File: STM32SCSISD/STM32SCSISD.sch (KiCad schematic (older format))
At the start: 19 parts, among them J1 SERIAL_DEBUG, J2 SWD, J3 USB, J4 SCSI, J5 ACTIVITYLED, J6 AMP FLOPPY PWR, J7 Micro_SD_Card_Det_Hirose_DM3AT, U1 STM32F103C8Tx, U2 MIC5504-3.3YM5, Y1 8MHz

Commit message: Pre-review of schematic.
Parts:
- added C10, C6, C7, C8, C9: 0.1u, symbol Device:C_Small
- added C3, C4, C5: 1u, symbol Device:C_Small
- added R1, R2: 22, symbol Device:R_Small
- added R10, R11, R6, R9: 10k, symbol Device:R_Small
- added R3: 4.7k, symbol Device:R_Small
- added R5: 470, symbol Device:R_Small
- added R7, R8: 47k, symbol Device:R_Small
- gave numbers to parts that had none: 3
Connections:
- net labels added: +5V, RESET, SD_CLK, SD_CS, SD_MISO, SD_MOSI, SERIAL_RX, SERIAL_TX, SWDCLK, SWDIO, UNIT_SEL2, USB+, USB-
- wire segments 114 -> 254
- no-connect marks 0 -> 7
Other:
- moved on the sheet: J6, JP1, JP2, JP3, JP5, JP6

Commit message: Hope this board looks nice!
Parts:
- removed R10, R11, R9: 10k, symbol Device:R_Small
- added C11: 47u, Capacitor_THT:CP_Radial_D5.0mm_P2.50mm, symbol Device:CP_Small
- added JP7: UNITSEL0, Connector_PinHeader_2.54mm:PinHeader_1x02_P2.54mm_Vertical, symbol Device:Jumper
- added JP8: UNITSEL1, Connector_PinHeader_2.54mm:PinHeader_1x02_P2.54mm_Vertical, symbol Device:Jumper
- C1, C10, C2, C3, C4, C5, C6, C7, C8, C9: footprint (none) -> Capacitor_SMD:C_0805_2012Metric
- J1: footprint (none) -> Connector_PinHeader_2.54mm:PinHeader_1x03_P2.54mm_Vertical
- J2, J3: footprint (none) -> Connector_PinHeader_2.54mm:PinHeader_1x04_P2.54mm_Vertical
- J4: footprint (none) -> Connector_IDC:IDC-Header_2x25_P2.54mm_Vertical
- J5, JP3, JP4, JP5, JP6: footprint (none) -> Connector_PinHeader_2.54mm:PinHeader_1x02_P2.54mm_Vertical
- J6: footprint (none) -> General:TE_MATE-N-LOK_350211-1_1x04_P5.08mm_Vertical
- J7: footprint (none) -> Connector_Card:microSD_HC_Hirose_DM3AT-SF-PEJM5
- JP1: value UNITSEL0 -> IMAGE_SEL0; footprint (none) -> Connector_PinHeader_2.54mm:PinHeader_1x02_P2.54mm_Vertical
- JP2: value UNITSEL1 -> IMAGE_SEL1; footprint (none) -> Connector_PinHeader_2.54mm:PinHeader_1x02_P2.54mm_Vertical
- R1, R2, R3, R4, R5, R6, R7, R8: footprint (none) -> Resistor_SMD:R_0805_2012Metric_Pad1.15x1.40mm_HandSolder
- Y1: footprint (none) -> Crystal:Crystal_HC49-U_Vertical
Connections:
- net labels added: IMAGE_SEL0, IMAGE_SEL1
- wire segments 254 -> 244
- no-connect marks 7 -> 10
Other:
- moved on the sheet: JP1, JP2

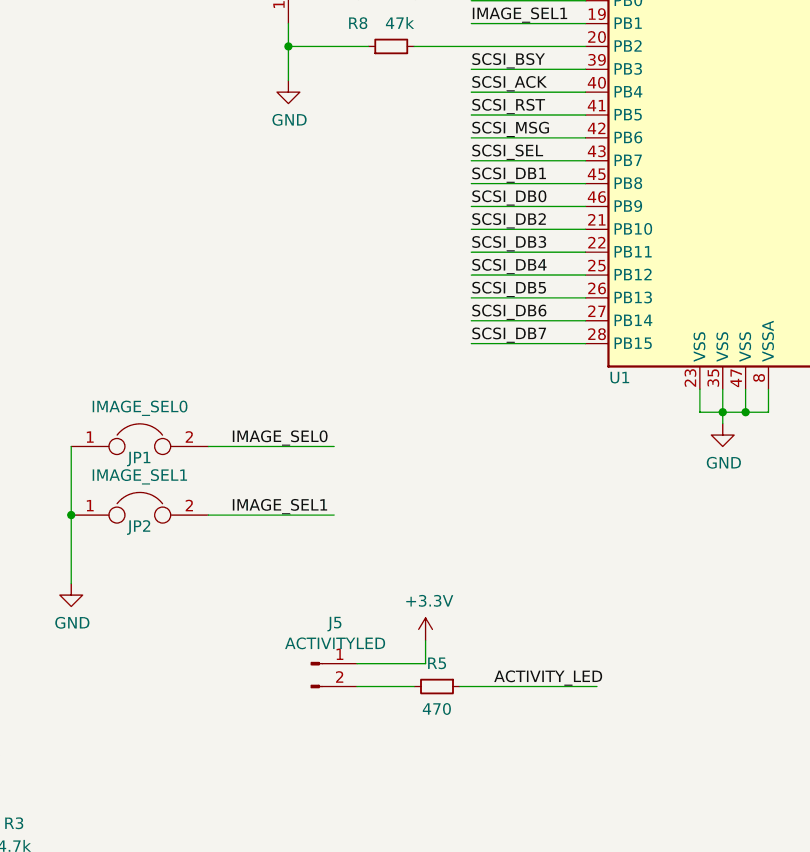
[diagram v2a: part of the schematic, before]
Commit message: Fixed the two SCSI databus bit that was mixed up. Added a 5mm LED instead of connector.
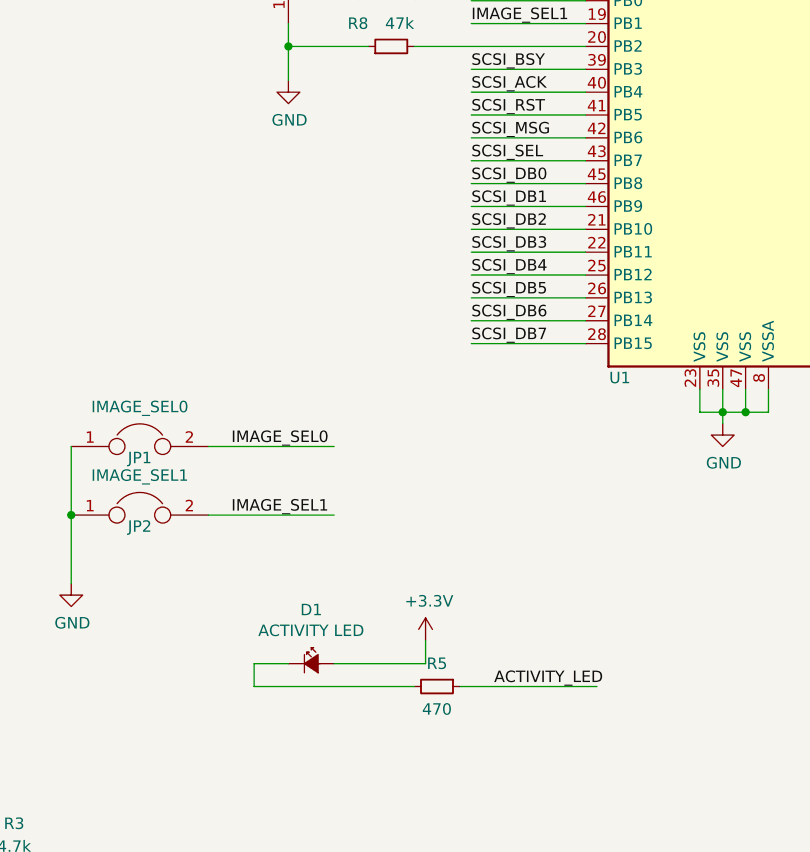
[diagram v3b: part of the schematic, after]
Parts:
- removed J5: ACTIVITYLED, Connector_PinHeader_2.54mm:PinHeader_1x02_P2.54mm_Vertical, symbol Connector:Conn_01x02_Male
- added D1: ACTIVITY LED, symbol Device:LED_Small_ALT
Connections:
- wire segments 244 -> 246
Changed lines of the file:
@@
-$EndComp
-$Comp
-L Connector:Conn_01x04_Male J3
-U 1 1 5FC2CB36
-P 1500 6850
-F 0 "J3" H 1606 7128 50  0000 C CNN
-F 1 "USB" H 1606 7037 50  0000 C CNN
-F 2 "Connector_PinHeader_2.54mm:PinHeader_1x04_P2.54mm_Vertical" H 1500 6850 50  0001 C CNN
-F 3 "~" H 1500 6850 50  0001 C CNN
-	1    1500 6850
-	1    0    0    -1
 $EndComp
 $Comp
@@
 F 3 "~" H 6450 6050 50  0001 C CNN
 	1    6450 6050
-	1    0    0    -1
-$EndComp
-$Comp
-L Connector:Conn_01x02_Male J5
-U 1 1 5FC2D24F
-P 3850 5800
-F 0 "J5" H 3956 5978 50  0000 C CNN
-F 1 "ACTIVITYLED" H 3956 5887 50  0000 C CNN
-F 2 "Connector_PinHeader_2.54mm:PinHeader_1x02_P2.54mm_Vertical" H 3850 5800 50  0001 C CNN
-F 3 "~" H 3850 5800 50  0001 C CNN
-	1    3850 5800
 	1    0    0    -1
 $EndComp
@@
 $EndComp
 Wire Wire Line
-	1700 6750 1950 6750
-Wire Wire Line
-	1700 7050 1800 7050
-Wire Wire Line
-	1800 7050 1800 7150
-Wire Wire Line
 	1650 6000 2200 6000
 Wire Wire Line
@@
 	2400 6450 2400 6500
 Wire Wire Line
-	1950 6450 1950 6750
-Wire Wire Line
 	2400 6700 2400 6950
 Connection ~ 2400 6950
@@
 Wire Wire Line
 	1700 6850 2050 6850
-Wire Wire Line
-	1700 6950 2050 6950
 $Comp
 L power:+5V #PWR08
@@
 $EndComp
 Wire Wire Line
-	4050 5800 4350 5800
-Wire Wire Line
 	4350 5800 4350 5700
-Wire Wire Line
-	4050 5900 4300 5900
 Wire Wire Line
 	4500 5900 5100 5900
@@
 Wire Wire Line
 	3750 3100 3750 3000
+Text Label 4550 3700 0    50   ~ 0
+SCSI_DB0
 Text Label 4550 3800 0    50   ~ 0
-SCSI_DB0
-Text Label 4550 3700 0    50   ~ 0
 SCSI_DB1
 Text Label 4550 3900 0    50   ~ 0
@@
 Wire Wire Line
 	7650 2350 8200 2350
+$Comp
+L Device:LED_Small_ALT D1
+U 1 1 5FEA5AEA
+P 3850 5800
+F 0 "D1" H 3850 6035 50  0000 C CNN
+F 1 "ACTIVITY LED" H 3850 5944 50  0000 C CNN
+F 2 "" V 3850 5800 50  0001 C CNN
+F 3 "~" V 3850 5800 50  0001 C CNN
+	1    3850 5800
+	1    0    0    -1
+$EndComp
+Wire Wire Line
+	3950 5800 4350 5800
+Wire Wire Line
+	3600 5900 3600 5800
+Wire Wire Line
+	3600 5800 3750 5800
+Wire Wire Line
+	3600 5900 4300 5900
+Wire Wire Line
+	1700 7050 1800 7050
+Wire Wire Line
+	1800 7050 1800 7150
+Wire Wire Line
+	1700 6950 2050 6950
+Wire Wire Line
+	1950 6450 1950 6750
+Wire Wire Line
+	1700 6750 1950 6750
+$Comp
+L Connector:Conn_01x04_Male J3
+U 1 1 5FC2CB36
+P 1500 6850
+F 0 "J3" H 1606 7128 50  0000 C CNN
+F 1 "USB" H 1606 7037 50  0000 C CNN
+F 2 "Connector_PinHeader_2.54mm:PinHeader_1x04_P2.54mm_Vertical" H 1500 6850 50  0001 C CNN
+F 3 "~" H 1500 6850 50  0001 C CNN
+	1    1500 6850
+	1    0    0    -1
+$EndComp
 $EndSCHEMATC

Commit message: Fixed the layout so that now it in sync with schematic. DB0 and DB1 is now corrected.
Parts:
- D1: footprint (none) -> LED_THT:LED_D5.0mm
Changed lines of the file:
@@
 F 0 "D1" H 3850 6035 50  0000 C CNN
 F 1 "ACTIVITY LED" H 3850 5944 50  0000 C CNN
-F 2 "" V 3850 5800 50  0001 C CNN
+F 2 "LED_THT:LED_D5.0mm" V 3850 5800 50  0001 C CNN
 F 3 "~" V 3850 5800 50  0001 C CNN
 	1    3850 5800
